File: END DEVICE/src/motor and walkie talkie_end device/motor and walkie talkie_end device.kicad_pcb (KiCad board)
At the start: 2 copper layers, 86.9 x 88.7 mm, 127 parts, among them IC1 LM4871MX, IC2 BQ24616RGER, IC4 TPS55340RTER, J1 ICSP, J2 FTDI_CONN, J3 speaker_conn, J4 Barrel_Jack_Switch, J5 Motor_Out, J6 BATT_CONN, Q1 DMP6185SE, Q2 DMP6185SE, Q3 IRF540NPBF, Q4 IRF540NPBF, Q5 IRF540NPBF, Q6 DMP6185SE, SW1 SW_Push, SW2 SW_Push, SW3 SW_Push, SW4 SW_Push, SW5 SW_Push, SW6 SW_SPDT, U1 ATmega328P-MU, U2 Ai-Thinker-Ra-02, U3 SA818-1W, U4 LP_Filter, U5 MCP41010, U6 LM1117-3.3(, U9 L4931ABDT50, Y1 16MHz

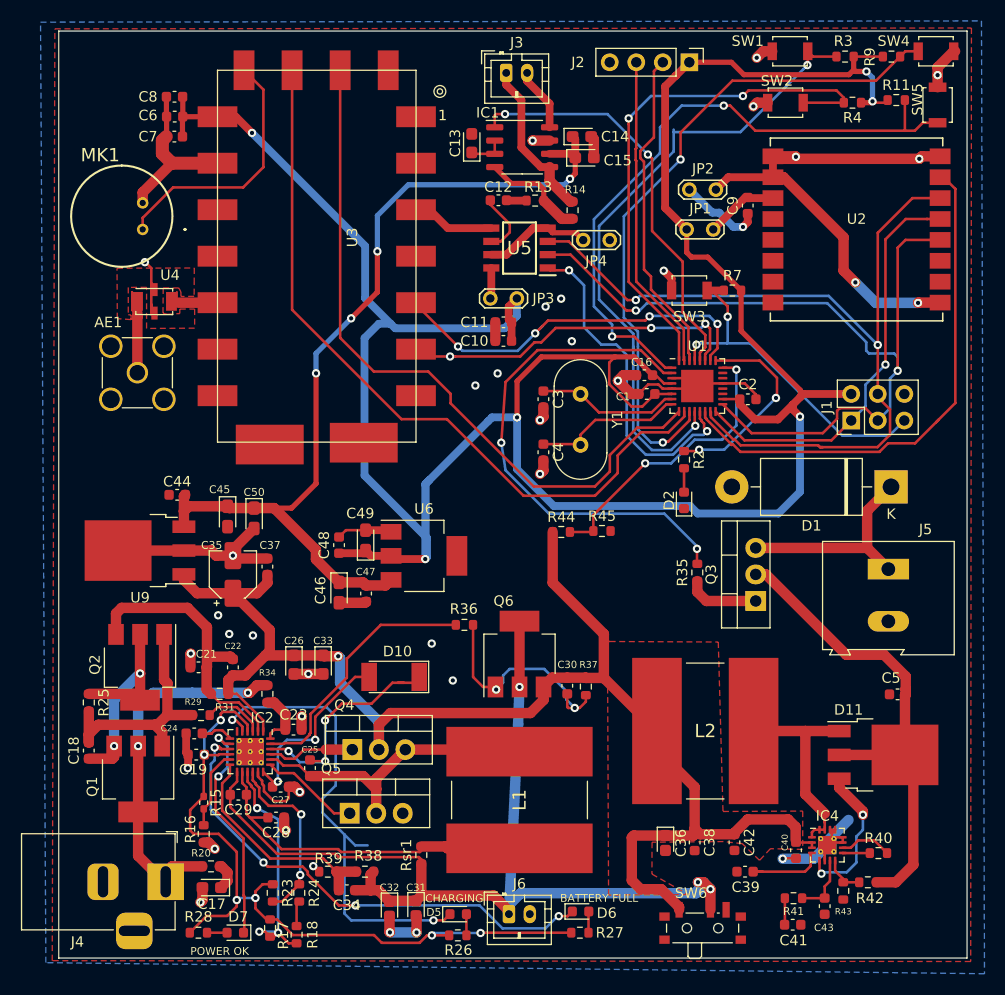
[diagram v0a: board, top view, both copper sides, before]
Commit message: Version 2 compressed board
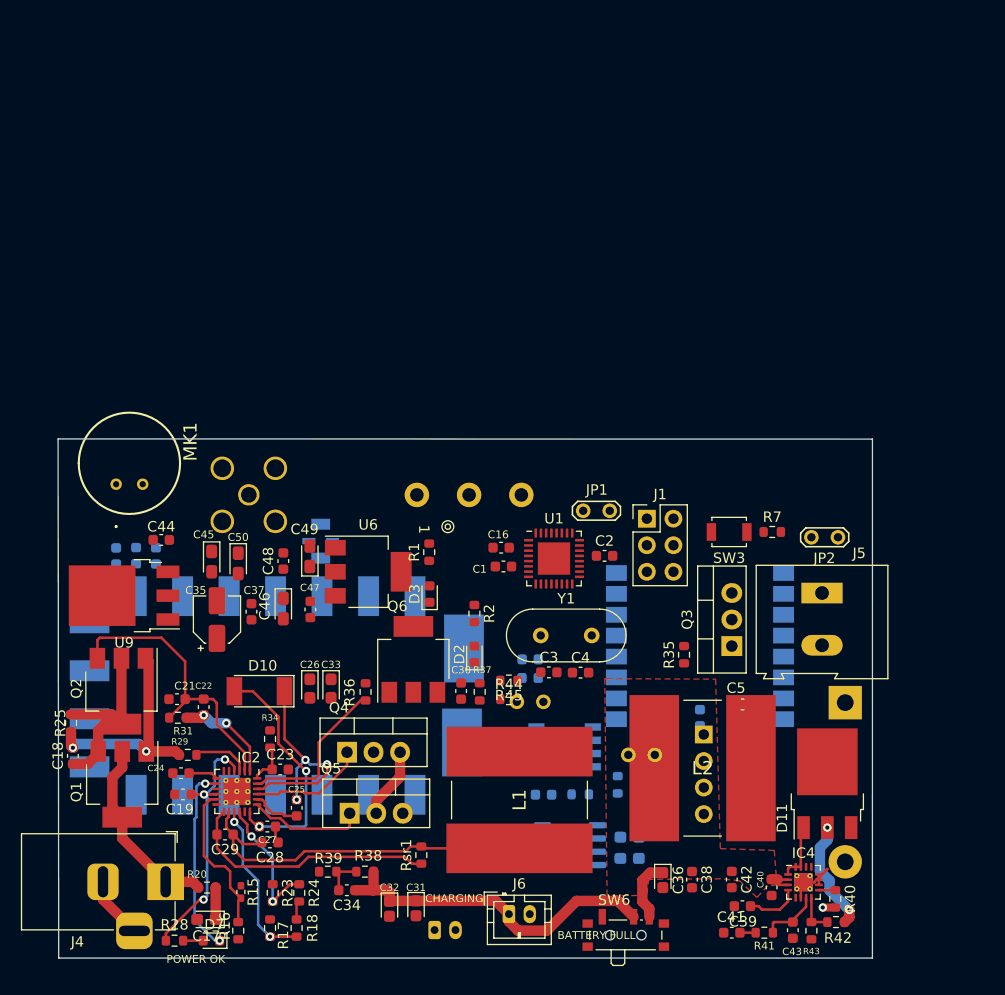
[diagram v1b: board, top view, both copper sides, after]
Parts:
- removed D5, D6: LED, LED_SMD:LED_0603_1608Metric
- removed R11, R26, R27, R3, R4, R9: 10k, Resistor_SMD:R_0603_1608Metric
- removed SW1, SW2, SW4, SW5: SW_Push, Button_Switch_SMD:SW_SPST_B3U-1000P
- added D3: LED, LED_SMD:LED_0603_1608Metric, F.Cu at (47.5, 162.7)
- added R1: 10k, Resistor_SMD:R_0603_1608Metric, F.Cu at (47.5, 158.7)
- added RV1: R_POT, Potentiometer_THT:Potentiometer_Alps_RK163_Single_Horizontal, B.Cu at (46.3, 153.2)
- AE1, C10, C11, C12, C13, C14, C15, C6, C7, C8, C9, D1, IC1, J2, J3, JP3, JP4, R13, R14, U2, U3, U4, U5: moved to B.Cu
- moved J3 82.3 mm to (48.0, 194.8)
- moved U3 76.1 mm to (15.0, 181.9), turned to 0 degrees
- moved C14 69.2 mm to (66.7, 188.0)
- moved C13 67.6 mm to (56.1, 186.9), turned to 270 degrees
- moved IC1 67.0 mm to (61.0, 186.7)
- moved C15 65.2 mm to (66.7, 185.9)
- moved J2 64.4 mm to (73.8, 176.1), turned to 180 degrees
- moved C12 57.1 mm to (58.4, 181.9)
- moved R13 57.0 mm to (61.9, 181.8)
- moved R14 55.2 mm to (65.5, 180.9), turned to 90 degrees
- moved JP4 49.5 mm to (69.1, 178.1)
- moved C9 49.2 mm to (73.4, 174.5)
- moved U5 47.9 mm to (60.5, 177.3)
- moved C8 44.0 mm to (21.3, 159.0), turned to 270 degrees
- moved U2 42.6 mm to (73.4, 167.6), turned to 180 degrees
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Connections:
- IC2 pad 5: /POWER sheet 1/STAT1 -> (no net)
- IC2 pad 9: /POWER sheet 1/STAT2 -> (no net)
- SW6 pad 1: BATT_IN -> (no net)
- SW6 pad 3: (no net) -> BATT_IN
- U1 pad 1: /FREQ- -> (no net)
- U1 pad 11: /VOL- -> (no net)
- U1 pad 12: /VOL+ -> (no net)
- U1 pad 23: (no net) -> /VOL
- U1 pad 32: /FREQ+ -> (no net)
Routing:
- net +3V3: track 278.4 -> 0.00 mm, vias 6 -> 0
- net GND: track 146.4 -> 16.8 mm, vias 33 -> 1
- net BATT_IN: track 138.1 -> 19.8 mm, vias 1 -> 2
- net +5V: track 87.0 -> 0.00 mm, vias 4 -> 0
- net MOSI: track 82.8 -> 0.00 mm, vias 2 -> 0
- net SCK: track 79.5 -> 0.00 mm, vias 2 -> 0
- net MCURX: track 72.4 -> 0.00 mm
- net MCU_TX: track 68.4 -> 0.00 mm
- net /VOL-: track 64.4 -> 0.00 mm, vias 2 -> 0
- net /FREQ-: track 62.4 -> 0.00 mm, vias 2 -> 0
- net /VOL+: track 62.2 -> 0.00 mm, vias 2 -> 0
- net /FREQ+: track 51.5 -> 0.00 mm, vias 2 -> 0
- net lora_SS: track 50.8 -> 0.00 mm
- net MOTOR_DRV: track 49.6 -> 0.00 mm, vias 2 -> 0
- net /COMMUNICATION/Lora_GND: track 49.2 -> 0.00 mm, vias 4 -> 0
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- removed copper zone on B.Cu, net GND
- removed copper zone on F.Cu, net GND
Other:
- board size 86.9 x 88.7 mm -> 77.9 x 49.7 mm

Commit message: latest update
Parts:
- J2, JP3, JP4: moved to F.Cu
- L1, L2: footprint Remote_devices:SDR1307680KL -> Remote_devices:ASPI-7318-6R8M-T
- R44: value 10K -> 28.2k
- R45: value 14K -> 10
- RV1: footprint Potentiometer_THT:Potentiometer_Alps_RK163_Single_Horizontal -> Potentiometer_THT:Potentiometer_Piher_PC-16_Single_Horizontal
- moved RV1 30.2 mm to (76.5, 152.6)
- moved JP1 26.9 mm to (76.1, 177.8)
- moved AE1 26.4 mm to (56.6, 152.1)
- moved J2 26.0 mm to (71.5, 150.2), turned to 270 degrees
- moved JP2 20.0 mm to (76.1, 174.2), turned to 0 degrees
- moved JP4 13.7 mm to (55.5, 179.9), turned to 90 degrees
- moved U2 13.3 mm to (75.3, 180.8)
- moved C9 13.1 mm to (86.1, 177.8), turned to 180 degrees
- moved C7 9.30 mm to (23.1, 151.5), turned to 90 degrees
- moved C8 7.75 mm to (19.2, 151.5), turned to 90 degrees
- moved C6 7.62 mm to (21.1, 151.6), turned to 90 degrees
- moved U3 7.49 mm to (14.4, 174.4)
- moved C11 6.56 mm to (63.1, 173.5)
- moved C5 6.38 mm to (83.5, 175.5)
- moved C10 5.74 mm to (62.9, 169.0)
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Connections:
- U1 pad 1: (no net) -> MOTOR_DRV
- U1 pad 2: MOTOR_DRV -> (no net)
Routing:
- net +BATT: track 59.1 -> 0.00 mm
- net Net-(C28-Pad2): track 35.6 -> 0.00 mm
- net Net-(C21-Pad1): track 28.3 -> 0.00 mm
- net /POWER sheet 1/vref: track 25.1 -> 0.00 mm, vias 3 -> 0
- net /POWER sheet 1/REGN: track 23.2 -> 0.00 mm, vias 2 -> 0
- net /POWER sheet 1/BTST: track 22.0 -> 0.00 mm, vias 3 -> 0
- net Net-(C18-Pad2): track 21.5 -> 0.00 mm, vias 2 -> 0
- net BATT_IN: track 19.8 -> 0.00 mm, vias 2 -> 0
- net Net-(C18-Pad1): track 19.0 -> 0.00 mm
- net Net-(J4-Pad1): track 18.4 -> 0.00 mm
- net /POWER sheet 1/~PG: track 18.1 -> 0.00 mm, vias 2 -> 0
- net GND: track 16.8 -> 0.00 mm, vias 1 -> 0
- net /POWER sheet 1/ISET2: track 15.9 -> 0.00 mm, vias 2 -> 0
- net Net-(IC2-Pad23): track 15.5 -> 0.00 mm
- net /POWER sheet 1/ISET1: track 14.8 -> 0.00 mm
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
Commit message: latest update
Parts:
- moved JP1 14.0 mm to (88.4, 184.4), turned to 90 degrees
- moved JP2 13.3 mm to (88.6, 178.9), turned to 90 degrees
- moved D11 1.88 mm to (82.2, 182.4)
- moved L2 1.37 mm to (73.9, 184.0)
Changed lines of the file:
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@@
   )
   (module Package_TO_SOT_SMD:TO-252-3_TabPin2 (layer F.Cu)
-    (at 83.99 181.91 90)
+    (at 82.17 182.37 90)
     (descr "TO-252 / DPAK SMD package, http://www.infineon.com/cms/en/product/packages/PG-TO252/PG-TO252-3-1/")
     (tags "DPAK TO-252 DPAK-3 TO-252-3 SOT-428")
@@
   )
   (module TestPoint:TestPoint_2Pads_Pitch2.54mm_Drill0.8mm (layer F.Cu)
-    (at 76.07 177.77)
+    (at 88.42 184.44 90)
     (descr "Test point with 2 pins, pitch 2.54mm, drill diameter 0.8mm")
     (tags "CONN DEV")
     (attr virtual)
-    (fp_text reference JP1 (at 1.3 -2) (layer F.SilkS)
-      (effects (font (size 1 1) (thickness 0.15)))
-    )
-    (fp_text value Jumper (at 1.27 2) (layer F.Fab)
+    (fp_text reference JP1 (at 1.3 -2 90) (layer F.SilkS)
+      (effects (font (size 1 1) (thickness 0.15)))
+    )
+    (fp_text value Jumper (at 1.27 2 90) (layer F.Fab)
       (effects (font (size 1 1) (thickness 0.15)))
     )
@@
     (fp_line (start 3.15 1.15) (end 3.8 0.5) (layer F.CrtYd) (width 0.05))
     (fp_line (start -0.65 1.15) (end 3.15 1.15) (layer F.CrtYd) (width 0.05))
-    (fp_text user %R (at 1.3 -2) (layer F.Fab)
-      (effects (font (size 1 1) (thickness 0.15)))
-    )
-    (pad 2 thru_hole circle (at 2.54 0) (size 1.4 1.4) (drill 0.8) (layers *.Cu *.Mask)
+    (fp_text user %R (at 1.3 -2 90) (layer F.Fab)
+      (effects (font (size 1 1) (thickness 0.15)))
+    )
+    (pad 2 thru_hole circle (at 2.54 0 90) (size 1.4 1.4) (drill 0.8) (layers *.Cu *.Mask)
       (net 6 /COMMUNICATION/Lora_3.3V))
-    (pad 1 thru_hole circle (at 0 0) (size 1.4 1.4) (drill 0.8) (layers *.Cu *.Mask)
+    (pad 1 thru_hole circle (at 0 0 90) (size 1.4 1.4) (drill 0.8) (layers *.Cu *.Mask)
       (net 2 +3V3))
   )
   (module TestPoint:TestPoint_2Pads_Pitch2.54mm_Drill0.8mm (layer F.Cu)
-    (at 76.09 174.21)
+    (at 88.58 178.92 90)
     (descr "Test point with 2 pins, pitch 2.54mm, drill diameter 0.8mm")
     (tags "CONN DEV")
     (attr virtual)
-    (fp_text reference JP2 (at 1.3 -2) (layer F.SilkS)
-      (effects (font (size 1 1) (thickness 0.15)))
-    )
-    (fp_text value Jumper (at 1.27 2) (layer F.Fab)
+    (fp_text reference JP2 (at 1.3 -2 90) (layer F.SilkS)
+      (effects (font (size 1 1) (thickness 0.15)))
+    )
+    (fp_text value Jumper (at 1.27 2 90) (layer F.Fab)
       (effects (font (size 1 1) (thickness 0.15)))
     )
@@
     (fp_line (start -1.03 0.4) (end -1.03 -0.4) (layer F.SilkS) (width 0.15))
     (fp_line (start -1.03 -0.4) (end -0.53 -0.9) (layer F.SilkS) (width 0.15))
-    (fp_text user %R (at 1.3 -2) (layer F.Fab)
-      (effects (font (size 1 1) (thickness 0.15)))
-    )
-    (pad 1 thru_hole circle (at 0 0) (size 1.4 1.4) (drill 0.8) (layers *.Cu *.Mask)
-      (net 3 GND))
-    (pad 2 thru_hole circle (at 2.54 0) (size 1.4 1.4) (drill 0.8) (layers *.Cu *.Mask)
+    (fp_text user %R (at 1.3 -2 90) (layer F.Fab)
+      (effects (font (size 1 1) (thickness 0.15)))
+    )
+    (pad 1 thru_hole circle (at 0 0 90) (size 1.4 1.4) (drill 0.8) (layers *.Cu *.Mask)
+      (net 3 GND))
+    (pad 2 thru_hole circle (at 2.54 0 90) (size 1.4 1.4) (drill 0.8) (layers *.Cu *.Mask)
       (net 54 /COMMUNICATION/Lora_GND))
   )
@@
   )
   (module Remote_devices:ASPI-7318-6R8M-T (layer F.Cu)
-    (at 75.08 184.72)
+    (at 73.92 184)
     (descr "Power Inductor, Wuerth Elektronik, WE-PD2, SMD, Typ L, , https://katalog.we-online.com/pbs/datasheet/74477510.pdf")
     (tags "Choke Power Inductor WE-PD2 TypL Wuerth")

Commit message: Everythinhg is set
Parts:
- L1: value 6.8uH_SDR1307-6R8ML -> 6.8uH_ASPI-7318-6R8M-T
- Y1: footprint Crystal:Crystal_HC49-4H_Vertical -> Crystal:Crystal_SMD_Abracon_ABM8G-4Pin_3.2x2.5mm
- moved R7 16.0 mm to (64.5, 159.4), turned to 270 degrees
- moved SW3 15.1 mm to (61.3, 159.2)
- moved C10 8.86 mm to (56.0, 174.5), turned to 90 degrees
- moved C2 7.56 mm to (68.8, 168.5)
- moved C1 6.26 mm to (59.3, 168.0)
- moved U1 6.24 mm to (64.0, 167.2)
- moved C16 6.23 mm to (59.2, 166.3)
- moved Y1 5.30 mm to (62.0, 173.4), turned to 180 degrees
- moved C3 4.23 mm to (59.0, 173.6), turned to 90 degrees
- moved R45 3.67 mm to (53.9, 174.4), turned to 270 degrees
- moved C11 3.28 mm to (59.8, 173.7)
- moved R44 2.32 mm to (55.9, 174.4)
- moved JP3 2.14 mm to (50.4, 177.6)
- moved R2 1.84 mm to (50.6, 165.9)
- moved C4 1.78 mm to (65.0, 173.4), turned to 270 degrees
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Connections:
- Y1 pad 1: Net-(C3-Pad1) -> Net-(C4-Pad1)
- Y1 pad 2: Net-(C4-Pad1) -> (no net)
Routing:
- net +3V3: track 0.00 -> 5.04 mm
- net GND: track 0.00 -> 3.63 mm

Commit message: All Set
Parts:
- moved U4 5.47 mm to (42.7, 149.5), turned to 180 degrees
- moved RV1 2.47 mm to (76.3, 155.0)
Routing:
- net Net-(C28-Pad2): track 0.00 -> 33.2 mm
- net +BATT: track 0.00 -> 28.1 mm
- net Net-(AE1-Pad1): track 0.00 -> 15.3 mm
- added copper zone on B.Cu, net GND
- added copper zone on B.Cu, net Net-(AE1-Pad1)
- added copper zone on B.Cu, net Net-(JP3-Pad2)
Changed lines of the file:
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@@
     (thickness 1.6)
     (drawings 14)
-    (tracks 11)
+    (tracks 38)
     (zones 0)
     (modules 118)
@@
   )
   (module Remote_devices:LFCN-530 (layer B.Cu)
-    (at 38.23 152.67)
+    (at 42.7 149.51 180)
     (fp_text reference U4 (at 3.63 0.966 180) (layer B.SilkS)
       (effects (font (size 1 1) (thickness 0.15)) (justify mirror))
@@
     (fp_line (start 4.29 -3.1) (end 0 -3.1) (layer Dwgs.User) (width 0.12))
     (fp_line (start 0 -3.1) (end 0 0) (layer Dwgs.User) (width 0.12))
-    (pad 1 smd rect (at 0 -0.65) (size 1.04 1.8) (drill (offset 0.52 -0.9)) (layers B.Cu B.Paste B.Mask)
+    (pad 1 smd rect (at 0 -0.65 180) (size 1.04 1.8) (drill (offset 0.52 -0.9)) (layers B.Cu B.Paste B.Mask)
       (net 1 "Net-(AE1-Pad1)"))
-    (pad 2 smd rect (at 4.29 -0.65) (size 1.04 1.8) (drill (offset -0.52 -0.9)) (layers B.Cu B.Paste B.Mask)
+    (pad 2 smd rect (at 4.29 -0.65 180) (size 1.04 1.8) (drill (offset -0.52 -0.9)) (layers B.Cu B.Paste B.Mask)
       (net 70 "Net-(U3-Pad12)"))
-    (pad 3 smd rect (at 1.84 0.2) (size 0.61 1.245) (drill (offset 0.305 -0.6225)) (layers B.Cu B.Paste B.Mask)
+    (pad 3 smd rect (at 1.84 0.2 180) (size 0.61 1.245) (drill (offset 0.305 -0.6225)) (layers B.Cu B.Paste B.Mask)
       (net 3 GND))
-    (pad 4 smd rect (at 1.84 -2.05) (size 0.61 1.245) (drill (offset 0.305 -0.6225)) (layers B.Cu B.Paste B.Mask)
+    (pad 4 smd rect (at 1.84 -2.05 180) (size 0.61 1.245) (drill (offset 0.305 -0.6225)) (layers B.Cu B.Paste B.Mask)
       (net 3 GND))
   )
@@
   )
   (module Potentiometer_THT:Potentiometer_Piher_PC-16_Single_Horizontal (layer B.Cu)
-    (at 76.54 152.57 90)
+    (at 76.27 155.03 90)
     (descr "Potentiometer, horizontal, Piher PC-16 Single, http://www.piher-nacesa.com/pdf/20-PC16v03.pdf")
     (tags "Potentiometer horizontal Piher PC-16 Single")
@@
     (effects (font (size 0.75 0.75) (thickness 0.15)))
   )
+  (segment (start 42.7 150.16) (end 42.7 151.07) (width 0.25) (layer B.Cu) (net 1))
+  (segment (start 42.7 151.07) (end 42.87 151.24) (width 0.25) (layer B.Cu) (net 1))
+  (segment (start 42.87 151.24) (end 48.11 151.24) (width 0.25) (layer B.Cu) (net 1))
+  (segment (start 48.95 152.08) (end 56.65 152.08) (width 0.25) (layer B.Cu) (net 1))
+  (segment (start 48.11 151.24) (end 48.95 152.08) (width 0.25) (layer B.Cu) (net 1))
   (segment (start 59.99 166.27) (end 60.24 166.27) (width 0.25) (layer F.Cu) (net 2))
   (segment (start 60.91 166.94) (end 61.5825 166.94) (width 0.25) (layer F.Cu) (net 2))
@@
   (segment (start 60.77359 167.44) (end 60.543599 167.210009) (width 0.25) (layer F.Cu) (net 3))
   (segment (start 59.380009 167.210009) (end 58.44 166.27) (width 0.25) (layer F.Cu) (net 3))
+  (segment (start 53 187.61) (end 53.98 188.59) (width 0.25) (layer F.Cu) (net 22))
+  (segment (start 46.88 187.61) (end 53 187.61) (width 0.25) (layer F.Cu) (net 22))
+  (segment (start 46.88 187.61) (end 45.89 187.61) (width 0.25) (layer F.Cu) (net 22))
+  (segment (start 45.89 187.61) (end 45.62 187.88) (width 0.25) (layer F.Cu) (net 22))
+  (segment (start 45.62 187.88) (end 29 187.88) (width 0.25) (layer F.Cu) (net 22))
+  (segment (start 29 187.88) (end 28.728 187.608) (width 0.25) (layer F.Cu) (net 22))
+  (segment (start 28.332 185.278) (end 28.332 183.4915) (width 0.25) (layer F.Cu) (net 22))
+  (segment (start 28.728 185.674) (end 28.332 185.278) (width 0.25) (layer F.Cu) (net 22))
+  (segment (start 28.728 187.608) (end 28.728 185.674) (width 0.25) (layer F.Cu) (net 22))
+  (segment (start 31.47 186.436) (end 30.736 186.436) (width 0.25) (layer F.Cu) (net 22))
+  (segment (start 29.974 185.674) (end 28.728 185.674) (width 0.25) (layer F.Cu) (net 22))
+  (segment (start 30.736 186.436) (end 29.974 185.674) (width 0.25) (layer F.Cu) (net 22))
+  (segment (start 46.228 189.912) (end 46.88 189.26) (width 0.25) (layer F.Cu) (net 23))
+  (segment (start 46.228 192.024) (end 46.228 189.912) (width 0.25) (layer F.Cu) (net 23))
+  (segment (start 46.88 189.26) (end 45.9 189.26) (width 0.25) (layer F.Cu) (net 23))
+  (segment (start 45.9 189.26) (end 45.2 188.56) (width 0.25) (layer F.Cu) (net 23))
+  (segment (start 45.2 188.56) (end 27.65 188.56) (width 0.25) (layer F.Cu) (net 23))
+  (segment (start 27.178 188.088) (end 27.178 185.674) (width 0.25) (layer F.Cu) (net 23))
+  (segment (start 27.65 188.56) (end 27.178 188.088) (width 0.25) (layer F.Cu) (net 23))
+  (segment (start 27.178 185.674) (end 27.178 185.672) (width 0.25) (layer F.Cu) (net 23))
+  (segment (start 27.832 185.018) (end 27.832 183.4915) (width 0.25) (layer F.Cu) (net 23))
+  (segment (start 27.178 185.672) (end 27.832 185.018) (width 0.25) (layer F.Cu) (net 23))
   (zone (net 16) (net_name BATT_IN) (layer F.Cu) (hatch edge 0.508)
     (connect_pads (clearance 0.508))
@@
       )
     )
+  )
+  (zone (net 55) (net_name "Net-(JP3-Pad2)") (layer B.Cu) (hatch edge 0.508)
+    (connect_pads (clearance 0.508))
+    (min_thickness 0.254)
+    (fill yes (arc_segments 32) (thermal_gap 0.508) (thermal_bridge_width 0.508))
+    (polygon
+      (pts
+        (xy 39.37 150.59) (xy 39.38 151.81) (xy 37.46 151.82) (xy 37.48 154.98) (xy 36.01 154.95)
+        (xy 35.95 150.58) (xy 39.36 150.58)
+      )
+    )
+  )
+  (zone (net 1) (net_name "Net-(AE1-Pad1)") (layer B.Cu) (hatch edge 0.508)
+    (connect_pads (clearance 0.508))
+    (min_thickness 0.254)
+    (fill yes (arc_segments 32) (thermal_gap 0.508) (thermal_bridge_width 0.508))
+    (polygon
+      (pts
+        (xy 41.801505 150.510098) (xy 56.65 151.48) (xy 56.78 152.56) (xy 56.3 152.61) (xy 41.86 151.85)
+        (xy 41.805143 150.597429) (xy 41.8 150.51) (xy 41.801318 150.510086) (xy 41.8 150.48)
+      )
+    )
+  )
+  (zone (net 3) (net_name GND) (layer B.Cu) (hatch edge 0.508)
+    (connect_pads (clearance 0.508))
+    (min_thickness 0.254)
+    (fill yes (arc_segments 32) (thermal_gap 0.508) (thermal_bridge_width 0.508))
+    (polygon
+      (pts
+        (xy 45.37 150.52) (xy 43.14 150.46) (xy 43.28 149.83) (xy 41.48 149.79) (xy 41.22 149.95)
+        (xy 41.24 152.02) (xy 41.57 152.26) (xy 45.64 152.18) (xy 45.73 153.16) (xy 37.57 153.13)
+        (xy 37.6 152) (xy 38.05 152) (xy 38.16 152.01) (xy 38.25 152.31) (xy 39.76 152.33)
+        (xy 39.89 152.11) (xy 39.86 149.81) (xy 38.16 149.84) (xy 37.9 150.36) (xy 35.74 150.34)
+        (xy 35.82 153.22) (xy 34.06 153.26) (xy 34.16 148.21) (xy 45.4 148.14)
+      )
+    )
